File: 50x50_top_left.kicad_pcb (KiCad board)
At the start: 2 copper layers, 48.9 x 48.3 mm, 97 parts, among them CON1 BARREL_JACK, CON2 USB_FEMALE_WITH_ID, CON3 USB_FEMALE_WITH_ID, J1 INTERCONNECT_3X1, J10 INTERCONNECT_3X1, J11 INTERCONNECT_3X1, J12 INTERCONNECT_3X1, J13 INTERCONNECT_3X1, J14 INTERCONNECT_3X1, J15 INTERCONNECT_3X1, J16 INTERCONNECT_3X1, J17 INTERCONNECT_3X1, J18 INTERCONNECT_3X1, J19 INTERCONNECT_3X1, J2 INTERCONNECT_3X1, J20 INTERCONNECT_3X1, J21 INTERCONNECT_3X1, J22 INTERCONNECT_3X1, J23 INTERCONNECT_3X1, J24 INTERCONNECT_3X1, J25 INTERCONNECT_3X1, J26 INTERCONNECT_3X1, J27 INTERCONNECT_3X1, J28 INTERCONNECT_3X1, J29 INTERCONNECT_3X1, J3 INTERCONNECT_3X1, J30 INTERCONNECT_3X1, J31 INTERCONNECT_3X1, J32 INTERCONNECT_3X1, J33 INTERCONNECT_3X1, J34 INTERCONNECT_3X1, J35 INTERCONNECT_3X1, J36 INTERCONNECT_3X1, J37 INTERCONNECT_3X1, J38 INTERCONNECT_3X1, J39 INTERCONNECT_3X1, J4 INTERCONNECT_3X1, J40 INTERCONNECT_3X1, J41 INTERCONNECT_3X1, J42 INTERCONNECT_3X1, J43 INTERCONNECT_3X1, J44 INTERCONNECT_3X1, J45 INTERCONNECT_3X1, J46 INTERCONNECT_3X1, J47 INTERCONNECT_3X1, J48 INTERCONNECT_3X1, J49 INTERCONNECT_3X1, J5 INTERCONNECT_3X1, J50 INTERCONNECT_3X1, J51 INTERCONNECT_3X1, J52 INTERCONNECT_3X1, J53 INTERCONNECT_3X1, J54 INTERCONNECT_3X1, J55 INTERCONNECT_3X1, J56 INTERCONNECT_3X1, J57 INTERCONNECT_3X1, J58 INTERCONNECT_3X1, J59 INTERCONNECT_3X1, J6 INTERCONNECT_3X1, J60 INTERCONNECT_3X1, J61 INTERCONNECT_3X1, J62 INTERCONNECT_3X1, J63 INTERCONNECT_3X1, J64 INTERCONNECT_3X1, J65 INTERCONNECT_2X1, J7 INTERCONNECT_3X1, J8 INTERCONNECT_3X1, J9 INTERCONNECT_3X1, P1 CONN_5, U1 LM7805CT

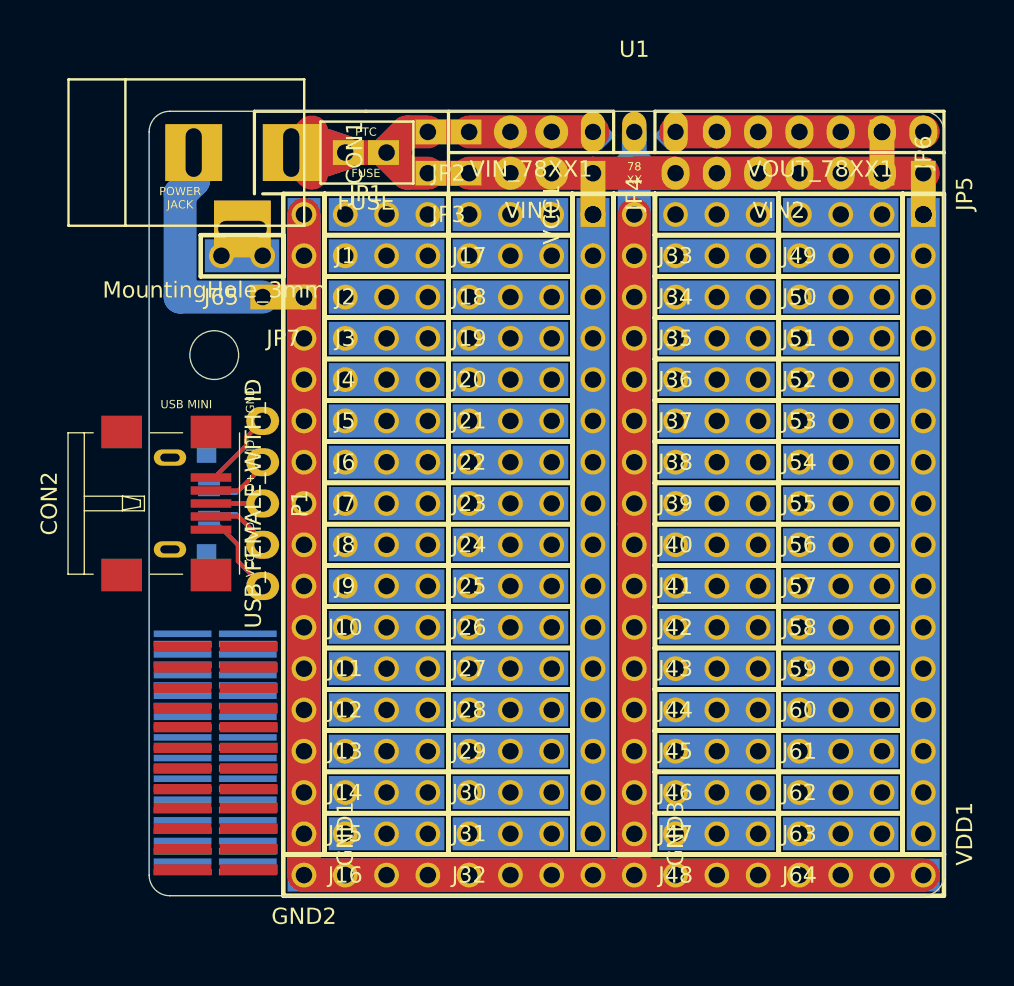
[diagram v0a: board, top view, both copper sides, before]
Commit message: completed top-left corner
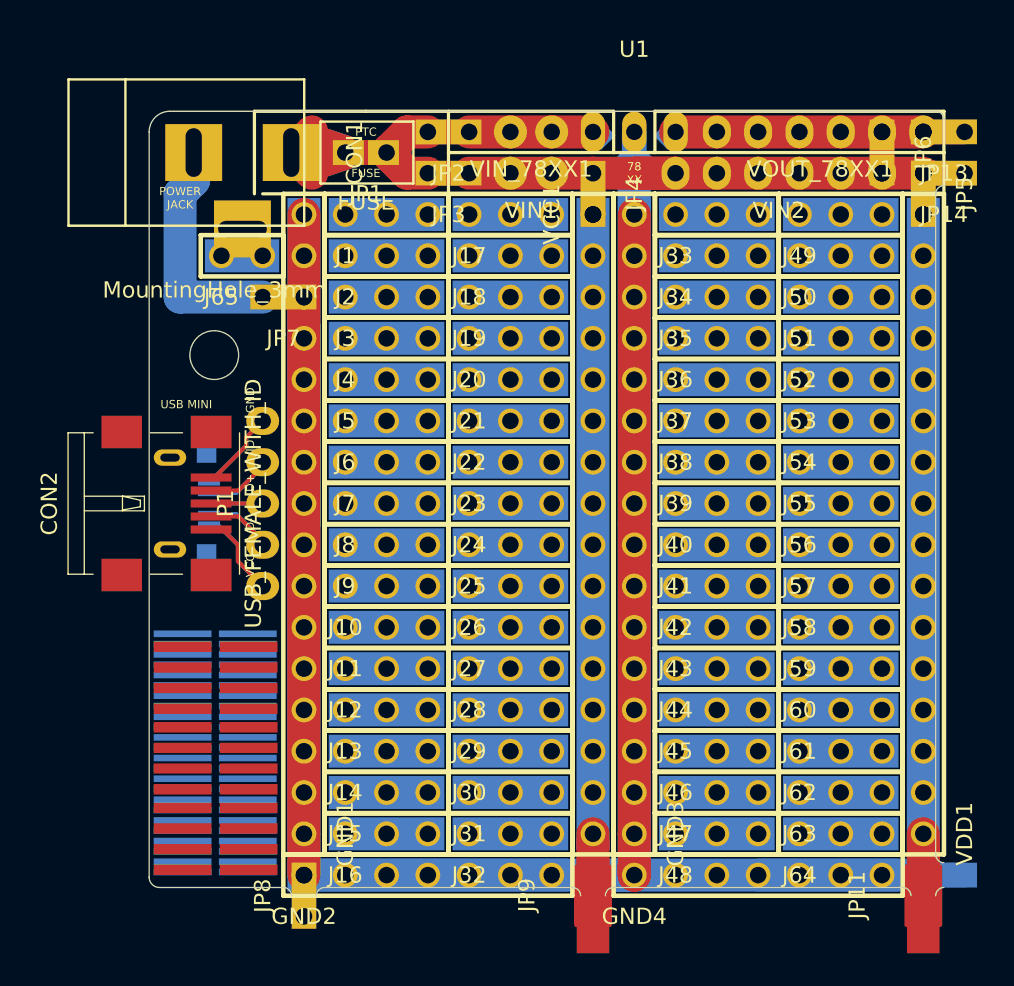
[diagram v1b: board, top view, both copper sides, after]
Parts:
- added GND4: INTERCONNECT_1X07, 2.54mm_Pin_Headers:Interconnect_1x07, F.Cu at (59.7, 69.8)
- added JP10: JUMPER, 2.54mm_Pin_Headers:Solder_Jumper_SMD_1x2, B.Cu at (77.5, 71.1)
- added JP11: JUMPER, Oddities:NetTie-I_Connected_SMD, F.Cu at (77.5, 71.1)
- added JP12: JUMPER, 2.54mm_Pin_Headers:Solder_Jumper_SMD_1x2_Shorted, B.Cu at (78.7, 69.8)
- added JP13: JUMPER, 2.54mm_Pin_Headers:Solder_Jumper_1x2_Shorted_T, F.Cu at (78.7, 24.1)
- added JP14: JUMPER, 2.54mm_Pin_Headers:Solder_Jumper_1x2_Shorted_T, F.Cu at (78.7, 26.7)
- added JP15: JUMPER, 2.54mm_Pin_Headers:Solder_Jumper_SMD_1x2_Shorted, B.Cu at (57.1, 71.1)
- added JP8: JUMPER, 2.54mm_Pin_Headers:Solder_Jumper_1x2, F.Cu at (39.4, 71.1)
- added JP9: JUMPER, Oddities:NetTie-I_Connected_SMD, F.Cu at (57.1, 71.1)
- GND1, GND3, VCC1, VDD1: value INTERCONNECT_16X1 -> INTERCONNECT_1X16
- GND2: value INTERCONNECT_16X1 -> INTERCONNECT_1X07; footprint 2.54mm_Pin_Headers:Interconnect_1x16 -> 2.54mm_Pin_Headers:Interconnect_1x07
- J1, J10, J11, J12, J13, J14, J15, J16, J17, J18, J19, J2, J20, J21, J22, J23, J24, J25, J26, J27, J28, J29, J3, J30, J31, J32, J33, J34, J35, J36, J37, J38, J39, J4, J40, J41, J42, J43, J44, J45, J46, J47, J48, J49, J5, J50, J51, J52, J53, J54, J55, J56, J57, J58, J59, J6, J60, J61, J62, J63, J64, J7, J8, J9: value INTERCONNECT_3X1 -> INTERCONNECT_1X03
- J65: value INTERCONNECT_2X1 -> INTERCONNECT_1X02
- P1: footprint Pin_Headers:Pin_Header_Straight_1x05 -> Socket_Strips:Socket_Strip_Straight_1x05
- turned P1 to 90 degrees
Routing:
- net Net-(C1-Pad2): track 248.0 -> 220.1 mm
- net Net-(JP4-Pad1): track 0.00 -> 2.54 mm
- net Net-(JP11-Pad1): track 0.00 -> 2.54 mm
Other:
- outline, holes or cut-outs redrawn

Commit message: fixed exposed frontside copper for GND traces
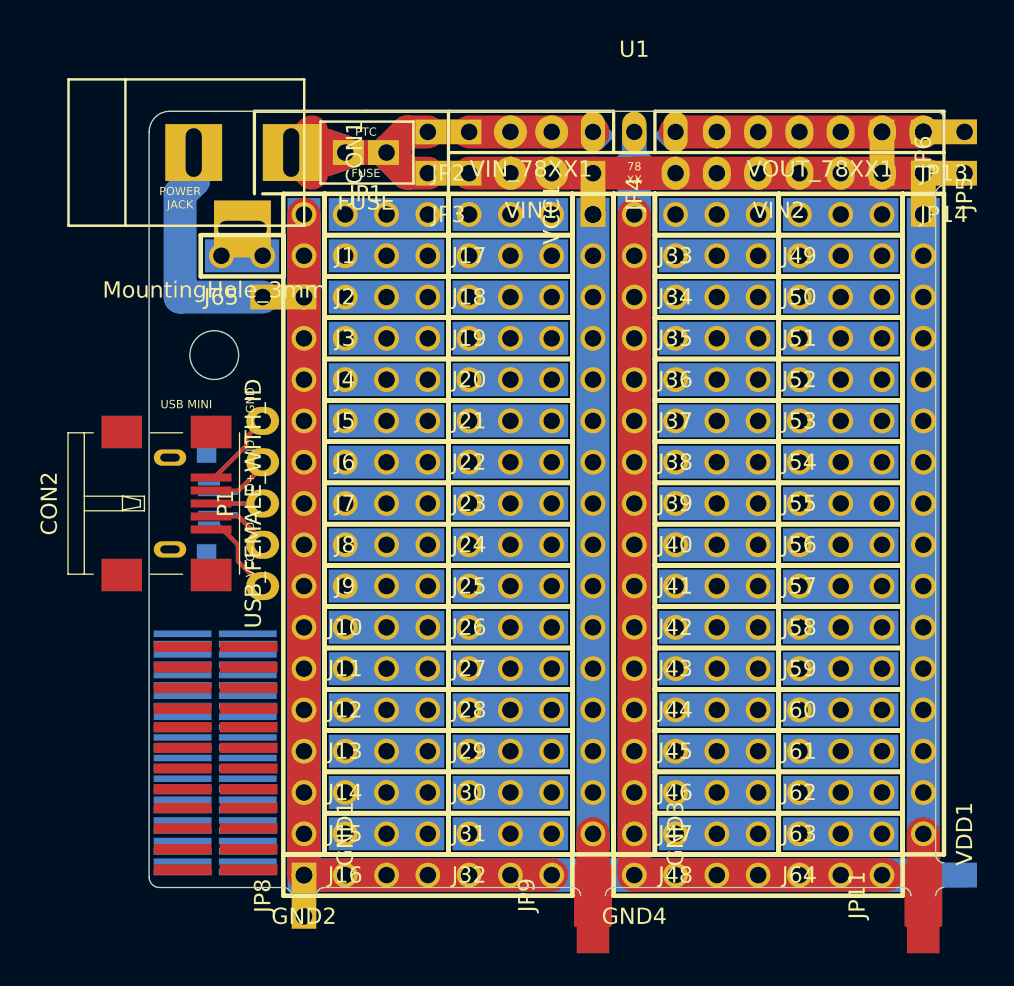
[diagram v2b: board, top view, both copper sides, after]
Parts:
- JP7: moved to B.Cu
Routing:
- net Net-(C1-Pad2): track 220.1 -> 281.6 mm
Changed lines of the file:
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@@
     (thickness 1.6)
     (drawings 64)
-    (tracks 84)
+    (tracks 88)
     (zones 0)
     (modules 106)
@@
   (layers
     (0 F.Cu signal)
-    (31 B.Cu signal)
+    (31 B.Cu signal hide)
     (32 B.Adhes user)
     (33 F.Adhes user)
@@
     (37 F.SilkS user)
     (38 B.Mask user hide)
-    (39 F.Mask user hide)
+    (39 F.Mask user)
     (40 Dwgs.User user)
     (41 Cmts.User user)
@@
     (pad_to_mask_clearance 0)
     (aux_axis_origin 0 0)
-    (visible_elements FFFCFF0F)
+    (visible_elements FFFCFD0F)
     (pcbplotparams
       (layerselection 0x010f0_80000001)
@@
       (net 2 "Net-(C1-Pad2)"))
   )
-  (module 2.54mm_Pin_Headers:Solder_Jumper_1x2_Shorted_T (layer F.Cu)
+  (module 2.54mm_Pin_Headers:Solder_Jumper_1x2_Shorted_T (layer B.Cu)
     (at 38.1 34.29)
-    (fp_text reference JP7 (at 0 2.54) (layer F.SilkS)
-      (effects (font (size 1 1) (thickness 0.15)))
-    )
-    (fp_text value JUMPER (at 0 -2.54) (layer F.SilkS) hide
-      (effects (font (size 1 1) (thickness 0.15)))
-    )
-    (fp_line (start 1.27 0) (end -1.27 0) (layer F.Cu) (width 1.524))
-    (pad 1 thru_hole rect (at -1.27 0) (size 1.905 1.524) (drill 1.016 (offset 0.1905 0)) (layers *.Cu *.Mask F.SilkS)
+    (fp_text reference JP7 (at 0 -2.54) (layer B.SilkS)
+      (effects (font (size 1 1) (thickness 0.15)) (justify mirror))
+    )
+    (fp_text value JUMPER (at 0 2.54) (layer B.SilkS) hide
+      (effects (font (size 1 1) (thickness 0.15)) (justify mirror))
+    )
+    (fp_line (start 1.27 0) (end -1.27 0) (layer B.Cu) (width 1.524))
+    (pad 1 thru_hole rect (at -1.27 0) (size 1.905 1.524) (drill 1.016 (offset 0.1905 0)) (layers *.Cu *.Mask B.SilkS)
       (net 5 "Net-(CON1-Pad2)"))
-    (pad 2 thru_hole rect (at 1.27 0) (size 1.905 1.524) (drill 1.016 (offset -0.1905 0)) (layers *.Cu *.Mask F.SilkS)
+    (pad 2 thru_hole rect (at 1.27 0) (size 1.905 1.524) (drill 1.016 (offset -0.1905 0)) (layers *.Cu *.Mask B.SilkS)
       (net 2 "Net-(C1-Pad2)"))
     (pad "" smd rect (at 0 0) (size 0.254 1.524) (layers *.Mask))
@@
   (segment (start 58.42 69.85) (end 39.37 69.85) (width 2.032) (layer B.Cu) (net 2))
   (segment (start 67.31 69.85) (end 77.47 69.85) (width 2.032) (layer B.Cu) (net 2))
+  (segment (start 77.47 69.85) (end 46.99 69.85) (width 2.032) (layer B.Cu) (net 2))
+  (segment (start 75.183998 69.85) (end 74.93 69.85) (width 2.032) (layer F.Cu) (net 2))
+  (segment (start 59.69 69.85) (end 75.183998 69.85) (width 2.032) (layer F.Cu) (net 2))
+  (segment (start 54.61 69.85) (end 39.37 69.85) (width 2.032) (layer F.Cu) (net 2))
   (segment (start 62.23 24.13) (end 64.77 24.13) (width 2.032) (layer F.Cu) (net 3))
   (segment (start 64.77 24.13) (end 67.31 24.13) (width 2.032) (layer F.Cu) (net 3))
@@
     (polygon
       (pts
-        (xy 78.486 70.866) (xy 60.706 70.866) (xy 58.674 70.866) (xy 40.386 70.866) (xy 38.354 70.866)
-        (xy 38.354 68.834) (xy 38.354 28.194) (xy 40.386 28.194) (xy 40.386 68.834) (xy 58.674 68.834)
-        (xy 58.674 28.194) (xy 60.706 28.194) (xy 60.706 68.834) (xy 78.486 68.834) (xy 78.486 70.866)
+        (xy 75.946 70.866) (xy 60.706 70.866) (xy 58.674 70.866) (xy 58.674 68.834) (xy 58.674 28.194)
+        (xy 60.706 28.194) (xy 60.706 68.834) (xy 75.946 68.834) (xy 75.946 70.866)
       )
     )
+  )
+  (zone (net 0) (net_name "") (layer F.Mask) (hatch edge 0.508)
+    (connect_pads (clearance 0.508))
+    (min_thickness 0.254)
+    (fill yes (arc_segments 16) (thermal_gap 0.508) (thermal_bridge_width 0.508))
+    (polygon
+      (pts
+        (xy 55.626 70.866) (xy 40.386 70.866) (xy 38.354 70.866) (xy 38.354 68.834) (xy 38.354 28.194)
+        (xy 40.386 28.194) (xy 40.386 68.834) (xy 55.626 68.834) (xy 55.626 70.866)
+      )
+    )

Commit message: moved shorted inter-board GND connection to center, switched av from Oddities:NetTie-I_Connected_SMD because they were asymmetrical and fixed pin header outlines
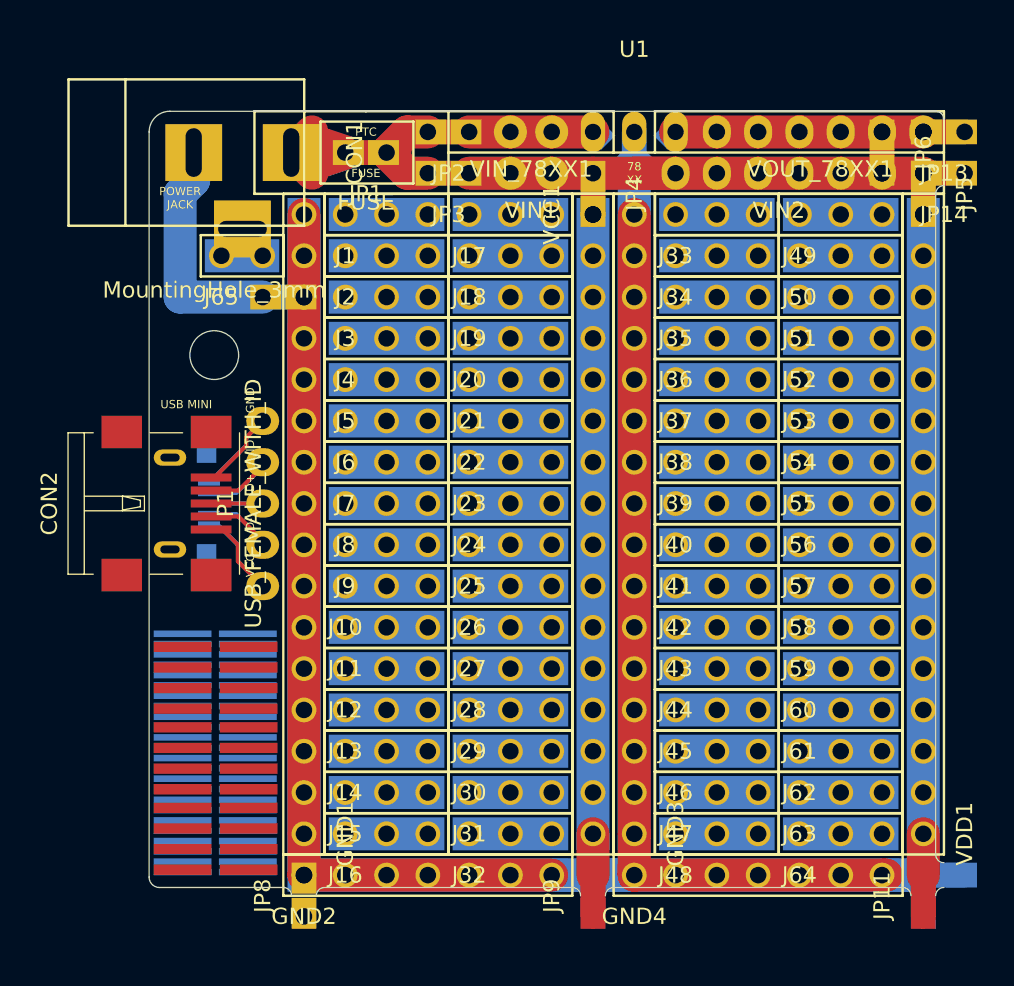
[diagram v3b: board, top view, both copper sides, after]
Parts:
- JP10: footprint 2.54mm_Pin_Headers:Solder_Jumper_SMD_1x2 -> 2.54mm_Pin_Headers:Solder_Jumper_SMD_1x2_Shorted
- JP11, JP9: footprint Oddities:NetTie-I_Connected_SMD -> 2.54mm_Pin_Headers:Solder_Jumper_SMD_1x2_Shorted
- JP15: footprint 2.54mm_Pin_Headers:Solder_Jumper_SMD_1x2_Shorted -> 2.54mm_Pin_Headers:Solder_Jumper_SMD_1x2

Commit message: rounded some corners
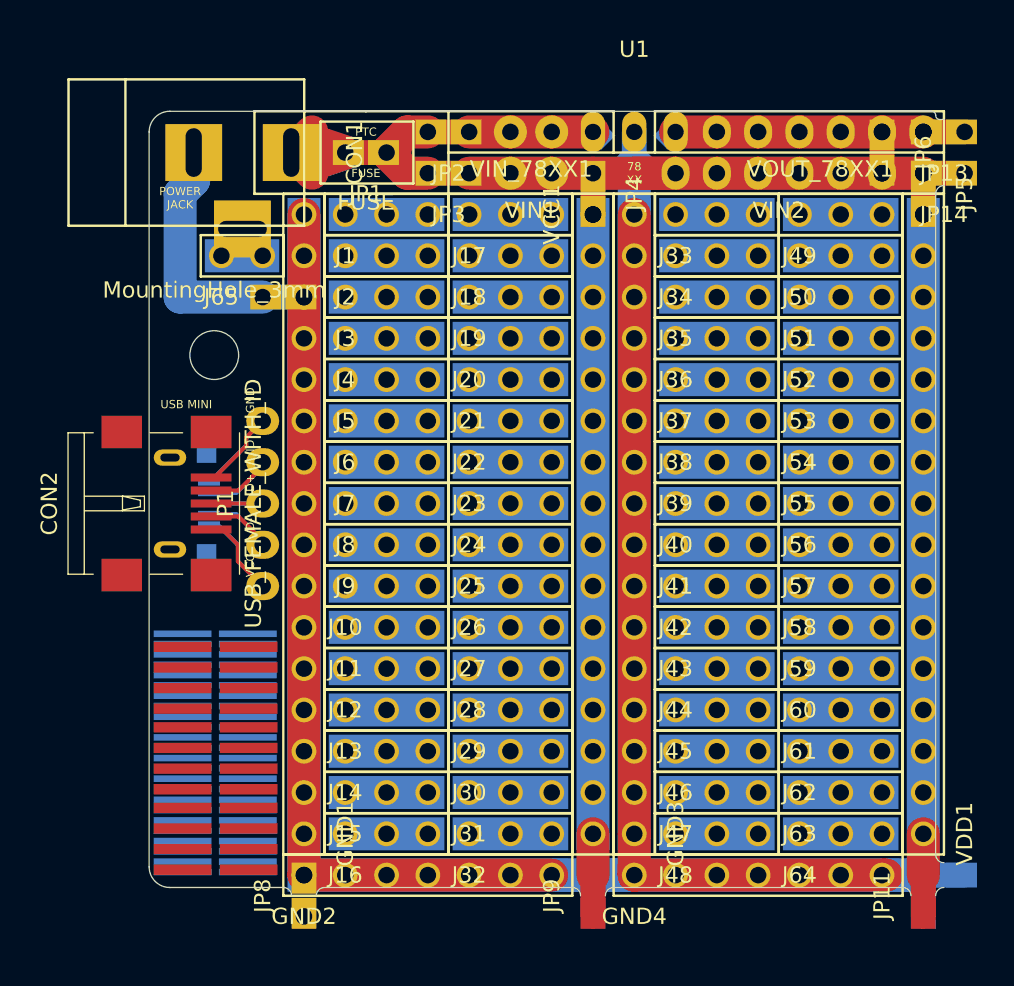
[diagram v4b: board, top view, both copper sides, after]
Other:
- outline, holes or cut-outs redrawn

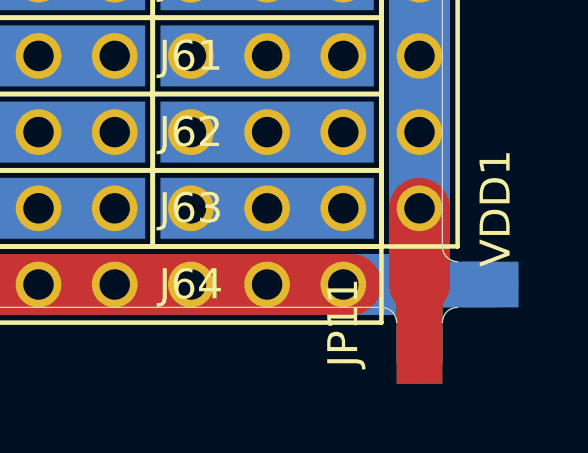
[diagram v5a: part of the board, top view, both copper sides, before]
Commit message: remove center border outline, because drilling it plated shorts PWR and GND
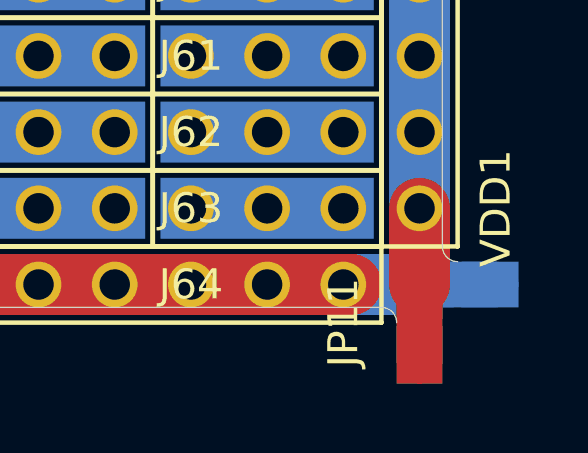
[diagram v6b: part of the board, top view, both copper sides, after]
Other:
- outline, holes or cut-outs redrawn
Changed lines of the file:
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@@
-(kicad_pcb (version 4) (host pcbnew "(2015-01-08 BZR 5360)-product")
+(kicad_pcb (version 4) (host pcbnew 4.0.2-stable)
   (general
     (links 341)
     (no_connects 10)
-    (area 18.365667 17.871 83.267572 73.5965)
+    (area 22.526 17.871 81.997572 75.424714)
     (thickness 1.6)
-    (drawings 66)
+    (drawings 65)
     (tracks 88)
     (zones 0)
@@
   (gr_line (start 76.2 70.612) (end 58.42 70.612) (angle 90) (layer Edge.Cuts) (width 0.0254))
   (gr_arc (start 76.2 71.12) (end 76.2 70.612) (angle 90) (layer Edge.Cuts) (width 0.0254))
-  (gr_arc (start 78.74 71.12) (end 78.232 71.12) (angle 90) (layer Edge.Cuts) (width 0.0254))
   (gr_arc (start 78.74 68.58) (end 78.74 69.088) (angle 90) (layer Edge.Cuts) (width 0.0254))
   (gr_line (start 78.232 27.94) (end 78.232 68.58) (angle 90) (layer Edge.Cuts) (width 0.0254))
